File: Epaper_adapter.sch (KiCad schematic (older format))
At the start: 26 parts, among them J3 Z5263CT-ND, Q1 AO3418

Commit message: Add files via upload
Trying to figure out whether to hook up the PGOOD and PWRGOOD and SHDN and so on.
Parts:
- added J? (x4): TEST_1P, symbol TEST_1P
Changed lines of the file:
@@
+	1    0    0    -1
+$EndComp
+$Comp
+L TEST_1P J?
+U 1 1 59E8F351
+P 3150 900
+F 0 "J?" H 3150 1100 50  0000 C CNN
+F 1 "TEST_1P" H 3150 1100 50  0001 C CNN
+F 2 "" H 3350 900 50  0001 C CNN
+F 3 "" H 3350 900 50  0001 C CNN
+	1    3150 900
+	1    0    0    -1
+$EndComp
+$Comp
+L TEST_1P J?
+U 1 1 59E8F46C
+P 3150 1200
+F 0 "J?" H 3150 1400 50  0000 C CNN
+F 1 "TEST_1P" H 3150 1400 50  0001 C CNN
+F 2 "" H 3350 1200 50  0001 C CNN
+F 3 "" H 3350 1200 50  0001 C CNN
+	1    3150 1200
+	1    0    0    -1
+$EndComp
+$Comp
+L TEST_1P J?
+U 1 1 59E8F4DC
+P 3750 1750
+F 0 "J?" H 3750 1950 50  0000 C CNN
+F 1 "TEST_1P" H 3750 1950 50  0001 C CNN
+F 2 "" H 3950 1750 50  0001 C CNN
+F 3 "" H 3950 1750 50  0001 C CNN
+	1    3750 1750
+	1    0    0    -1
+$EndComp
+$Comp
+L TEST_1P J?
+U 1 1 59E8F569
+P 3750 2150
+F 0 "J?" H 3750 2350 50  0000 C CNN
+F 1 "TEST_1P" H 3750 2350 50  0001 C CNN
+F 2 "" H 3950 2150 50  0001 C CNN
+F 3 "" H 3950 2150 50  0001 C CNN
+	1    3750 2150
 	1    0    0    -1
 $EndComp

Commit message: Add files via upload
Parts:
- added J39: TEST_1P, symbol TEST_1P
- gave numbers to parts that had none: 12
- renumbered C11 to C12, C12 to C13, C13 to C14, C14 to C15, C15 to C16, C16 to C17, C17 to C18, C18 to C19, C19 to C20, C20 to C21, C21 to C22, J3 to J31, R7 to R10
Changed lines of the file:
@@
 $EndDescr
 $Comp
-L CONN_01X34 J3
+L CONN_01X34 J31
 U 1 1 59C3EB0D
 P 5900 3300
-F 0 "J3" H 5900 5050 50  0000 C CNN
+F 0 "J31" H 5900 5050 50  0000 C CNN
 F 1 "Z5263CT-ND" V 6000 3300 50  0000 C CNN
 F 2 "" H 5900 3300 50  0001 C CNN
@@
 $EndComp
 $Comp
-L GND #PWR016
+L GND #PWR021
 U 1 1 59C3F01A
 P 5300 5350
-F 0 "#PWR016" H 5300 5100 50  0001 C CNN
+F 0 "#PWR021" H 5300 5100 50  0001 C CNN
 F 1 "GND" H 5300 5200 50  0000 C CNN
 F 2 "" H 5300 5350 50  0001 C CNN
@@
 GND
 $Comp
-L GND #PWR017
+L GND #PWR022
 U 1 1 59C401DC
 P 1400 4600
-F 0 "#PWR017" H 1400 4350 50  0001 C CNN
+F 0 "#PWR022" H 1400 4350 50  0001 C CNN
 F 1 "GND" H 1400 4450 50  0000 C CNN
 F 2 "" H 1400 4600 50  0001 C CNN
@@
 	1400 4500 1400 4600
 $Comp
-L C_Small C11
+L C_Small C12
 U 1 1 59C4291C
 P 1350 1850
-F 0 "C11" H 1360 1920 50  0000 L CNN
+F 0 "C12" H 1360 1920 50  0000 L CNN
 F 1 "1uF" H 1450 1850 50  0000 L CNN
 F 2 "" H 1350 1850 50  0001 C CNN
@@
 $EndComp
 $Comp
-L C_Small C12
+L C_Small C13
 U 1 1 59C42B0E
 P 1700 1850
-F 0 "C12" H 1710 1920 50  0000 L CNN
+F 0 "C13" H 1710 1920 50  0000 L CNN
 F 1 "1uF" H 1800 1850 50  0000 L CNN
 F 2 "" H 1700 1850 50  0001 C CNN
@@
 $EndComp
 $Comp
-L C_Small C13
+L C_Small C14
 U 1 1 59C42C29
 P 2500 1850
-F 0 "C13" H 2510 1920 50  0000 L CNN
+F 0 "C14" H 2510 1920 50  0000 L CNN
 F 1 "2.2uF" H 2600 1850 50  0000 L CNN
 F 2 "" H 2500 1850 50  0001 C CNN
@@
 $EndComp
 $Comp
-L C_Small C14
+L C_Small C15
 U 1 1 59C42E6A
 P 3350 1850
-F 0 "C14" H 3360 1920 50  0000 L CNN
+F 0 "C15" H 3360 1920 50  0000 L CNN
 F 1 "1uF" H 3450 1850 50  0000 L CNN
 F 2 "" H 3350 1850 50  0001 C CNN
@@
 $EndComp
 $Comp
-L C_Small C15
+L C_Small C16
 U 1 1 59C42EC1
 P 3150 2300
-F 0 "C15" H 3160 2370 50  0000 L CNN
+F 0 "C16" H 3160 2370 50  0000 L CNN
 F 1 "1uF" H 3250 2300 50  0000 L CNN
 F 2 "" H 3150 2300 50  0001 C CNN
@@
 $EndComp
 $Comp
-L GND #PWR018
+L GND #PWR023
 U 1 1 59C43106
 P 1350 2250
-F 0 "#PWR018" H 1350 2000 50  0001 C CNN
+F 0 "#PWR023" H 1350 2000 50  0001 C CNN
 F 1 "GND" H 1350 2100 50  0000 C CNN
 F 2 "" H 1350 2250 50  0001 C CNN
@@
 $EndComp
 $Comp
-L GND #PWR019
+L GND #PWR024
 U 1 1 59C4344F
 P 2500 2600
-F 0 "#PWR019" H 2500 2350 50  0001 C CNN
+F 0 "#PWR024" H 2500 2350 50  0001 C CNN
 F 1 "GND" H 2500 2450 50  0000 C CNN
 F 2 "" H 2500 2600 50  0001 C CNN
@@
 	2500 2200 2500 1950
 $Comp
-L GND #PWR020
+L GND #PWR025
 U 1 1 59C435DC
 P 3350 2000
-F 0 "#PWR020" H 3350 1750 50  0001 C CNN
+F 0 "#PWR025" H 3350 1750 50  0001 C CNN
 F 1 "GND" H 3350 1850 50  0000 C CNN
 F 2 "" H 3350 2000 50  0001 C CNN
@@
 GDR
 $Comp
-L R_Small R7
+L R_Small R10
 U 1 1 59C44064
 P 3050 1350
-F 0 "R7" H 3080 1370 50  0000 L CNN
+F 0 "R10" H 3080 1370 50  0000 L CNN
 F 1 "2.2R 1%" H 3080 1310 50  0000 L CNN
 F 2 "" H 3050 1350 50  0001 C CNN
@@
 $EndComp
 $Comp
-L GND #PWR021
+L GND #PWR026
 U 1 1 59C440D3
 P 3050 1500
-F 0 "#PWR021" H 3050 1250 50  0001 C CNN
+F 0 "#PWR026" H 3050 1250 50  0001 C CNN
 F 1 "GND" H 3050 1350 50  0000 C CNN
 F 2 "" H 3050 1500 50  0001 C CNN
@@
 Connection ~ 3050 1200
 $Comp
-L C_Small C16
+L C_Small C17
 U 1 1 59C44AA9
 P 1250 6750
-F 0 "C16" H 1260 6820 50  0000 L CNN
+F 0 "C17" H 1260 6820 50  0000 L CNN
 F 1 "1uF" H 1350 6750 50  0000 L CNN
 F 2 "" H 1250 6750 50  0001 C CNN
@@
 $EndComp
 $Comp
-L C_Small C17
+L C_Small C18
 U 1 1 59C44B40
 P 1650 6750
-F 0 "C17" H 1660 6820 50  0000 L CNN
+F 0 "C18" H 1660 6820 50  0000 L CNN
 F 1 "1uF" H 1750 6750 50  0000 L CNN
 F 2 "" H 1650 6750 50  0001 C CNN
@@
 $EndComp
 $Comp
-L C_Small C18
+L C_Small C19
 U 1 1 59C44B8C
 P 2050 6750
-F 0 "C18" H 2060 6820 50  0000 L CNN
+F 0 "C19" H 2060 6820 50  0000 L CNN
 F 1 "1uF" H 2150 6750 50  0000 L CNN
 F 2 "" H 2050 6750 50  0001 C CNN
@@
 $EndComp
 $Comp
-L C_Small C19
+L C_Small C20
 U 1 1 59C44BDF
 P 2450 6750
-F 0 "C19" H 2460 6820 50  0000 L CNN
+F 0 "C20" H 2460 6820 50  0000 L CNN
 F 1 "1uF" H 2550 6750 50  0000 L CNN
 F 2 "" H 2450 6750 50  0001 C CNN
@@
 $EndComp
 $Comp
-L C_Small C20
+L C_Small C21
 U 1 1 59C44C2D
 P 2800 6750
-F 0 "C20" H 2810 6820 50  0000 L CNN
+F 0 "C21" H 2810 6820 50  0000 L CNN
 F 1 "1uF" H 2900 6750 50  0000 L CNN
 F 2 "" H 2800 6750 50  0001 C CNN
@@
 $EndComp
 $Comp
-L C_Small C21
+L C_Small C22
 U 1 1 59C44C7C
 P 3150 6750
-F 0 "C21" H 3160 6820 50  0000 L CNN
+F 0 "C22" H 3160 6820 50  0000 L CNN
 F 1 "1uF" H 3250 6750 50  0000 L CNN
 F 2 "" H 3150 6750 50  0001 C CNN
@@
 $EndComp
 $Comp
-L GND #PWR022
+L GND #PWR027
 U 1 1 59C44CCD
 P 1250 7000
-F 0 "#PWR022" H 1250 6750 50  0001 C CNN
+F 0 "#PWR027" H 1250 6750 50  0001 C CNN
 F 1 "GND" H 1250 6850 50  0000 C CNN
 F 2 "" H 1250 7000 50  0001 C CNN
@@
 	5700 3850 5350 3850
 Wire Wire Line
-	5700 3950 5350 3950
+	5200 3950 5700 3950
 Wire Wire Line
 	5700 4050 5350 4050
@@
 NoConn ~ 5250 2750
 $Comp
-L TEST_1P J?
+L TEST_1P J34
 U 1 1 59CC61A6
 P 1750 3750
-F 0 "J?" H 1750 3950 50  0000 C CNN
+F 0 "J34" H 1750 3950 50  0000 C CNN
 F 1 "TEST_1P" H 1750 3950 50  0001 C CNN
 F 2 "" H 1950 3750 50  0001 C CNN
@@
 ~CS
 $Comp
-L TEST_1P J?
+L TEST_1P J32
 U 1 1 59E046D1
 P 1650 3450
-F 0 "J?" H 1650 3650 50  0000 C CNN
+F 0 "J32" H 1650 3650 50  0000 C CNN
 F 1 "TEST_1P" H 1650 3650 50  0001 C CNN
 F 2 "" H 1850 3450 50  0001 C CNN
@@
 $EndComp
 $Comp
-L TEST_1P J?
+L TEST_1P J33
 U 1 1 59E0474B
 P 1700 3600
-F 0 "J?" H 1700 3800 50  0000 C CNN
+F 0 "J33" H 1700 3800 50  0000 C CNN
 F 1 "TEST_1P" H 1700 3800 50  0001 C CNN
 F 2 "" H 1900 3600 50  0001 C CNN
@@
 $EndComp
 $Comp
-L TEST_1P J?
+L TEST_1P J35
 U 1 1 59E04A7A
 P 1800 3900
-F 0 "J?" H 1800 4100 50  0000 C CNN
+F 0 "J35" H 1800 4100 50  0000 C CNN
 F 1 "TEST_1P" H 1800 4100 50  0001 C CNN
 F 2 "" H 2000 3900 50  0001 C CNN
@@
 $EndComp
 $Comp
-L TEST_1P J?
+L TEST_1P J36
 U 1 1 59E04AD0
 P 1850 4050
-F 0 "J?" H 1850 4250 50  0000 C CNN
+F 0 "J36" H 1850 4250 50  0000 C CNN
 F 1 "TEST_1P" H 1850 4250 50  0001 C CNN
 F 2 "" H 2050 4050 50  0001 C CNN
@@
 $EndComp
 $Comp
-L TEST_1P J?
+L TEST_1P J37
 U 1 1 59E04B2D
 P 1900 4200
-F 0 "J?" H 1900 4400 50  0000 C CNN
+F 0 "J37" H 1900 4400 50  0000 C CNN
 F 1 "TEST_1P" H 1900 4400 50  0001 C CNN
 F 2 "" H 2100 4200 50  0001 C CNN
@@
 $EndComp
 $Comp
-L TEST_1P J?
+L TEST_1P J38
 U 1 1 59E05B20
 P 1400 4500
-F 0 "J?" H 1400 4700 50  0000 C CNN
+F 0 "J38" H 1400 4700 50  0000 C CNN
 F 1 "TEST_1P" H 1400 4700 50  0001 C CNN
 F 2 "" H 1600 4500 50  0001 C CNN
@@
 $EndComp
 $Comp
-L TEST_1P J?
+L TEST_1P J28
 U 1 1 59E4F023
 P 1700 1750
-F 0 "J?" H 1700 1950 50  0000 C CNN
+F 0 "J28" H 1700 1950 50  0000 C CNN
 F 1 "TEST_1P" H 1700 1950 50  0001 C CNN
 F 2 "" H 1900 1750 50  0001 C CNN
@@
 $EndComp
 $Comp
-L TEST_1P J?
+L TEST_1P J26
 U 1 1 59E8F351
 P 3150 900
-F 0 "J?" H 3150 1100 50  0000 C CNN
+F 0 "J26" H 3150 1100 50  0000 C CNN
 F 1 "TEST_1P" H 3150 1100 50  0001 C CNN
 F 2 "" H 3350 900 50  0001 C CNN
@@
 $EndComp
 $Comp
-L TEST_1P J?
+L TEST_1P J27
 U 1 1 59E8F46C
 P 3150 1200
-F 0 "J?" H 3150 1400 50  0000 C CNN
+F 0 "J27" H 3150 1400 50  0000 C CNN
 F 1 "TEST_1P" H 3150 1400 50  0001 C CNN
 F 2 "" H 3350 1200 50  0001 C CNN
@@
 $EndComp
 $Comp
-L TEST_1P J?
+L TEST_1P J29
 U 1 1 59E8F4DC
 P 3750 1750
-F 0 "J?" H 3750 1950 50  0000 C CNN
+F 0 "J29" H 3750 1950 50  0000 C CNN
 F 1 "TEST_1P" H 3750 1950 50  0001 C CNN
 F 2 "" H 3950 1750 50  0001 C CNN
@@
 $EndComp
 $Comp
-L TEST_1P J?
+L TEST_1P J30
 U 1 1 59E8F569
 P 3750 2150
-F 0 "J?" H 3750 2350 50  0000 C CNN
+F 0 "J30" H 3750 2350 50  0000 C CNN
 F 1 "TEST_1P" H 3750 2350 50  0001 C CNN
 F 2 "" H 3950 2150 50  0001 C CNN
@@
 	1    0    0    -1
 $EndComp
+$Comp
+L TEST_1P J39
+U 1 1 59EAAE72
+P 5200 3950
+F 0 "J39" H 5200 4150 50  0000 C CNN
+F 1 "TEST_1P" H 5200 4150 50  0001 C CNN
+F 2 "" H 5400 3950 50  0001 C CNN
+F 3 "" H 5400 3950 50  0001 C CNN
+	1    5200 3950
+	1    0    0    -1
+$EndComp

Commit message: Add files via upload
Working on the BOM and footprints.
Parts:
- added TP11, TP13, TP20, TP21, TP22, TP25: TEST_1P, Wire_Pads:SolderWirePad_single_1-2mmDrill, symbol TEST_1P
- C12, C13, C14, C15, C16, C17, C18, C19, C20, C21, C22: footprint (none) -> Capacitors_SMD:C_1206_HandSoldering
- L1: footprint (none) -> Inductors_SMD:L_Coilcraft_XAL5030
- Q1: footprint (none) -> TO_SOT_Packages_SMD:SOT-23
- TP12: renamed from J32; footprint (none) -> Wire_Pads:SolderWirePad_single_1-2mmDrill
- TP14: renamed from J28; footprint (none) -> Wire_Pads:SolderWirePad_single_1-2mmDrill
- TP15: renamed from J33; footprint (none) -> Wire_Pads:SolderWirePad_single_1-2mmDrill
- TP16: renamed from J34; footprint (none) -> Wire_Pads:SolderWirePad_single_1-2mmDrill
- TP17: renamed from J35; footprint (none) -> Wire_Pads:SolderWirePad_single_1-2mmDrill
- TP18: renamed from J36; footprint (none) -> Wire_Pads:SolderWirePad_single_1-2mmDrill
- TP19: renamed from J37; footprint (none) -> Wire_Pads:SolderWirePad_single_1-2mmDrill
- TP23: renamed from J26; footprint (none) -> Wire_Pads:SolderWirePad_single_1-2mmDrill
- TP24: renamed from J27; footprint (none) -> Wire_Pads:SolderWirePad_single_1-2mmDrill
- TP26: renamed from J29; footprint (none) -> Wire_Pads:SolderWirePad_single_1-2mmDrill
- TP27: renamed from J30; footprint (none) -> Wire_Pads:SolderWirePad_single_1-2mmDrill
- TP28: renamed from J39; footprint (none) -> Wire_Pads:SolderWirePad_single_1-2mmDrill
- TP29: renamed from J38; footprint (none) -> Wire_Pads:SolderWirePad_single_1-2mmDrill

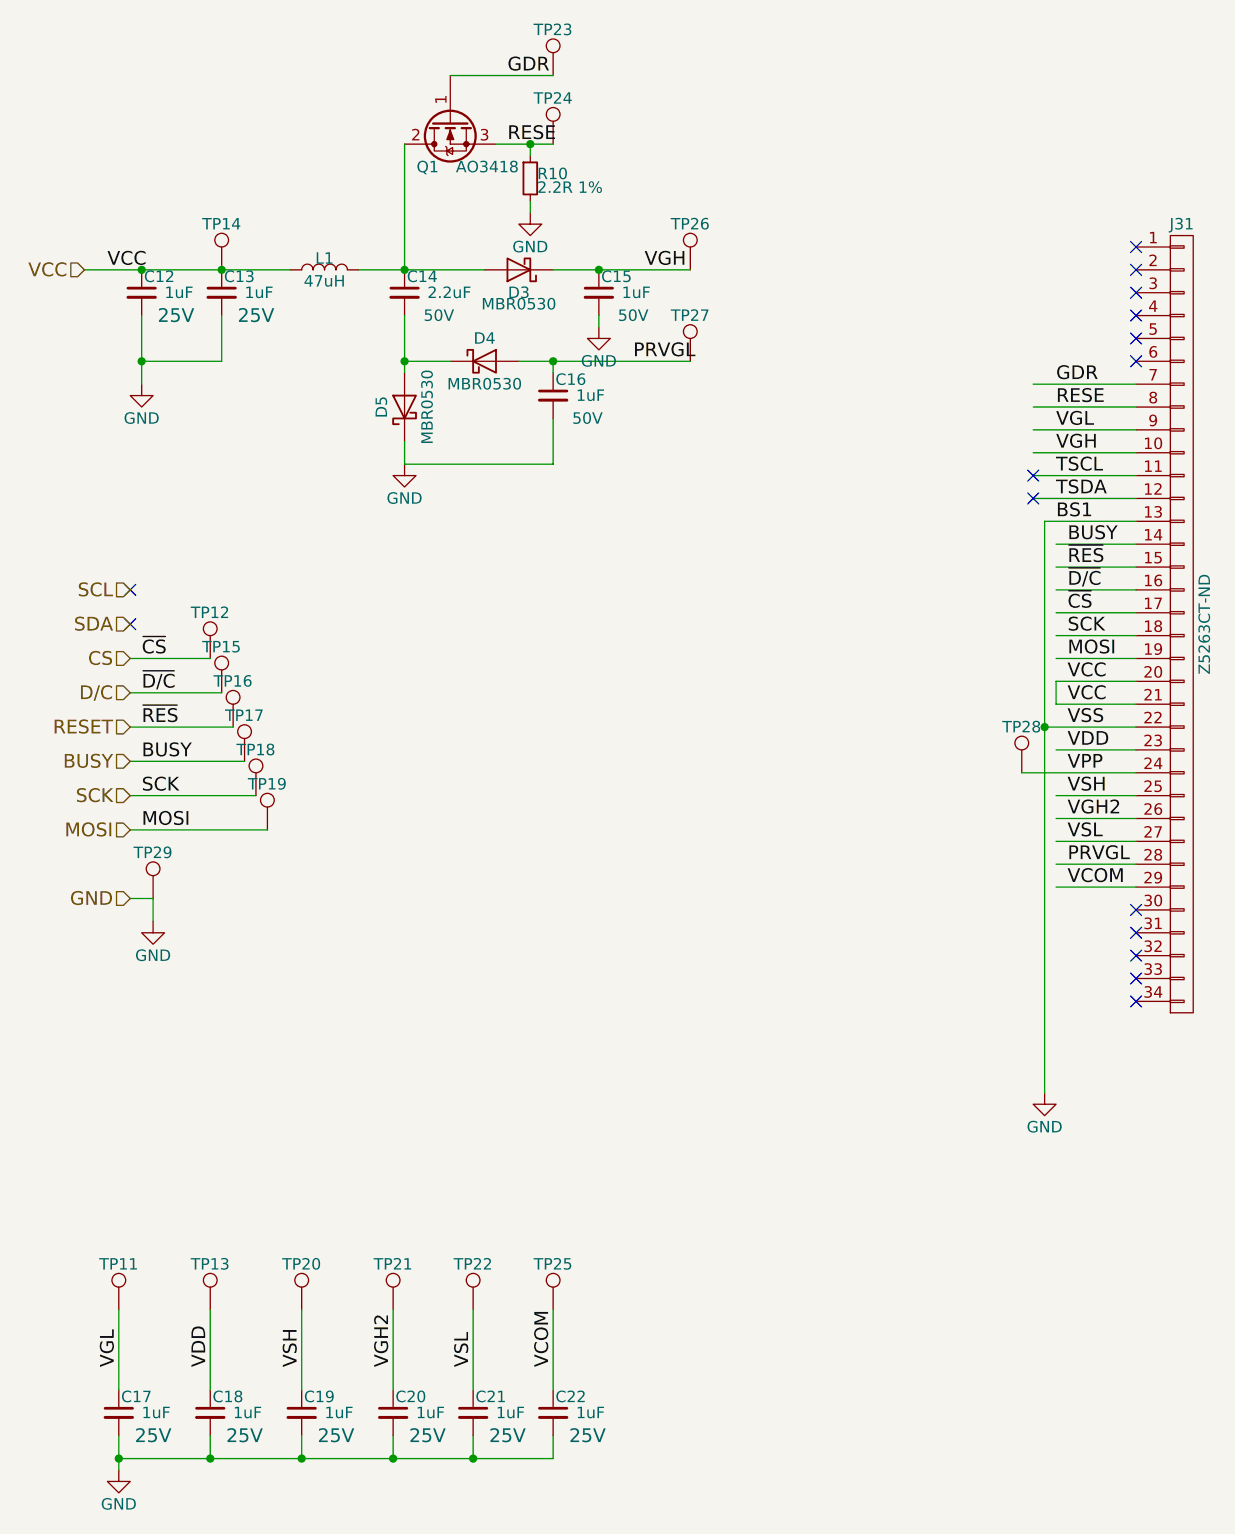
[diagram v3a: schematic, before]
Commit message: Add files via upload
Ready to do layout. All footprints correct, no board size chosen yet. Made outline for 6cm x 3.5cm e-paper.
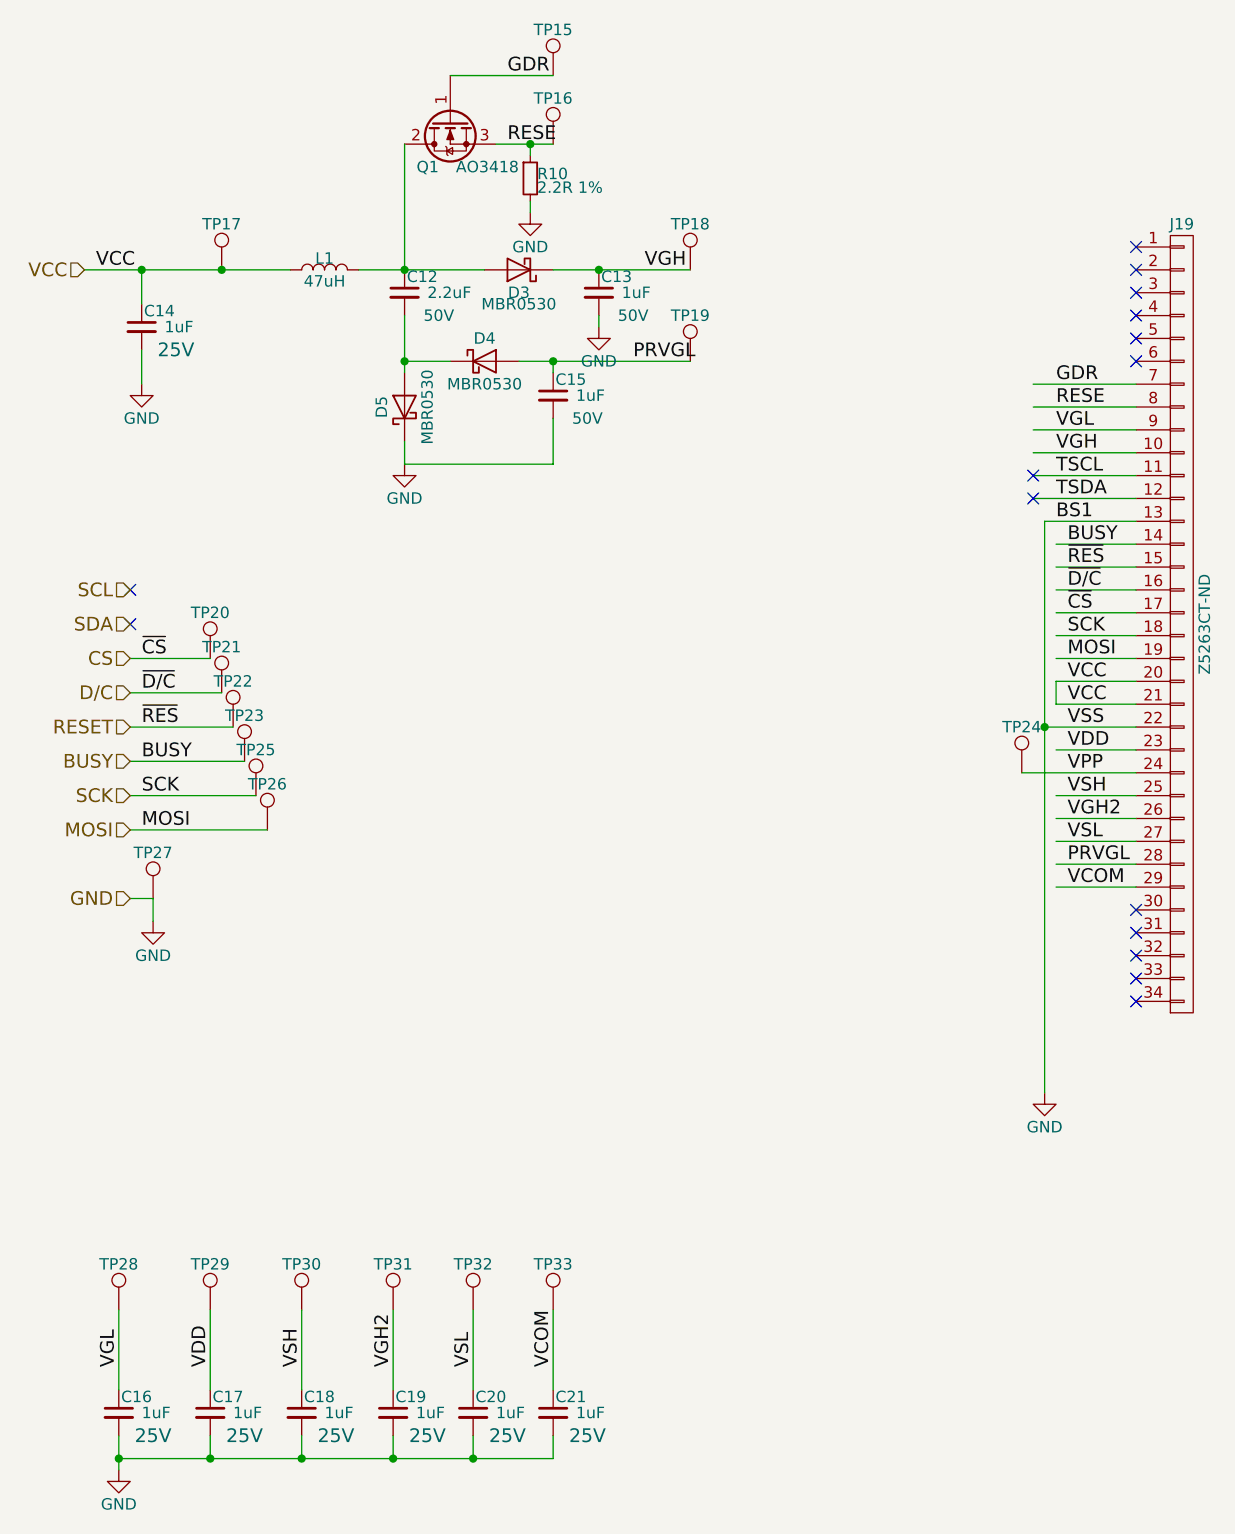
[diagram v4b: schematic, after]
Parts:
- removed C13: 1uF, Capacitors_SMD:C_1206_HandSoldering, symbol C_Small
- D3, D4, D5: footprint Diodes_SMD:SOD-123 -> Diodes_SMD:D_SOD-123
- J19: renamed from J31; footprint (none) -> CustomFootprints:FPC_34
- R10: footprint (none) -> Resistors_SMD:R_1206_HandSoldering
- TP15: renamed from TP23; footprint Wire_Pads:SolderWirePad_single_1-2mmDrill -> CustomFootprints:TestPointHole
- TP16: renamed from TP24; footprint Wire_Pads:SolderWirePad_single_1-2mmDrill -> CustomFootprints:TestPointHole
- TP17: renamed from TP14; footprint Wire_Pads:SolderWirePad_single_1-2mmDrill -> CustomFootprints:TestPointHole
- TP18: renamed from TP26; footprint Wire_Pads:SolderWirePad_single_1-2mmDrill -> CustomFootprints:TestPointHole
- TP19: renamed from TP27; footprint Wire_Pads:SolderWirePad_single_1-2mmDrill -> CustomFootprints:TestPointHole
- TP20: renamed from TP12; footprint Wire_Pads:SolderWirePad_single_1-2mmDrill -> CustomFootprints:TestPointHole
- TP21: renamed from TP15; footprint Wire_Pads:SolderWirePad_single_1-2mmDrill -> CustomFootprints:TestPointHole
- TP22: renamed from TP16; footprint Wire_Pads:SolderWirePad_single_1-2mmDrill -> CustomFootprints:TestPointHole
- TP23: renamed from TP17; footprint Wire_Pads:SolderWirePad_single_1-2mmDrill -> CustomFootprints:TestPointHole
- TP24: renamed from TP28; footprint Wire_Pads:SolderWirePad_single_1-2mmDrill -> CustomFootprints:TestPointHole
- TP25: renamed from TP18; footprint Wire_Pads:SolderWirePad_single_1-2mmDrill -> CustomFootprints:TestPointHole
- TP26: renamed from TP19; footprint Wire_Pads:SolderWirePad_single_1-2mmDrill -> CustomFootprints:TestPointHole
- TP27: renamed from TP29; footprint Wire_Pads:SolderWirePad_single_1-2mmDrill -> CustomFootprints:TestPointHole
- TP28: renamed from TP11; footprint Wire_Pads:SolderWirePad_single_1-2mmDrill -> CustomFootprints:TestPointHole
- TP29: renamed from TP13; footprint Wire_Pads:SolderWirePad_single_1-2mmDrill -> CustomFootprints:TestPointHole
- TP30: renamed from TP20; footprint Wire_Pads:SolderWirePad_single_1-2mmDrill -> CustomFootprints:TestPointHole
- TP31: renamed from TP21; footprint Wire_Pads:SolderWirePad_single_1-2mmDrill -> CustomFootprints:TestPointHole
- TP32: renamed from TP22; footprint Wire_Pads:SolderWirePad_single_1-2mmDrill -> CustomFootprints:TestPointHole
- TP33: renamed from TP25; footprint Wire_Pads:SolderWirePad_single_1-2mmDrill -> CustomFootprints:TestPointHole
- renumbered C14 to C12, C15 to C13, C12 to C14, C16 to C15, C17 to C16, C18 to C17, C19 to C18, C20 to C19, C21 to C20, C22 to C21
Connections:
- wire segments 65 -> 64
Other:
- moved on the sheet: C14
